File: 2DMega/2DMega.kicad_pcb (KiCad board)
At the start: 2 copper layers, 122.6 x 68.6 mm, 40 parts, among them J1 Conn_01x04_Male, J2 Conn_01x04_Female, J3 Conn_01x04_Male, J4 Conn_01x04_Female, P1 Power, P10 CONN_01X01, P11 CONN_01X01, P12 CONN_01X01, P13 CONN_01X01, P2 Analog, P3 Analog, P4 Digital, P5 PWM, P6 PWM, P7 Communication, P8 CONN_01X01, P9 CONN_01X01, U1 HDSP-A153

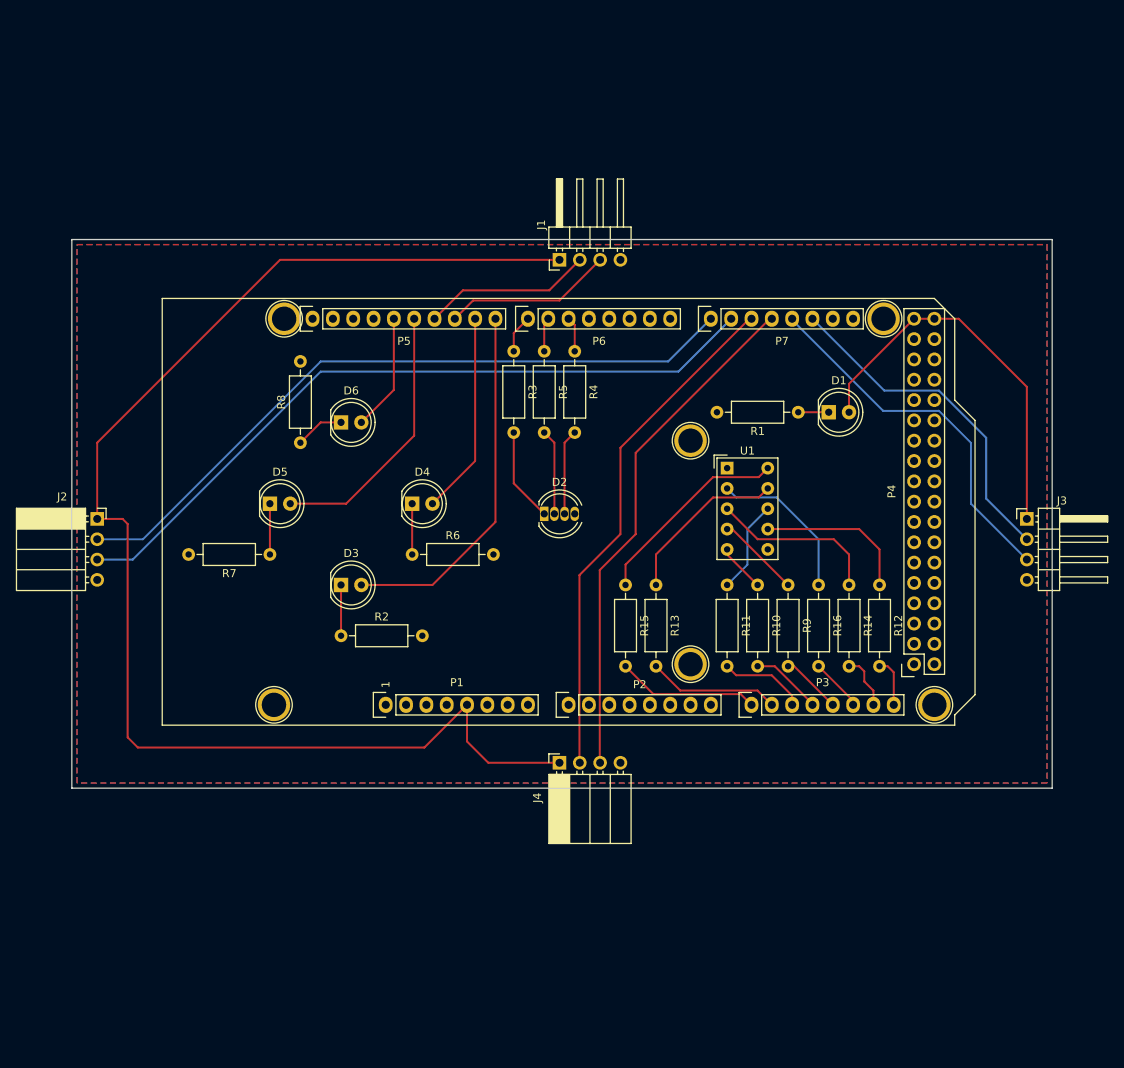
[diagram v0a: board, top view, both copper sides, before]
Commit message: Changed to square
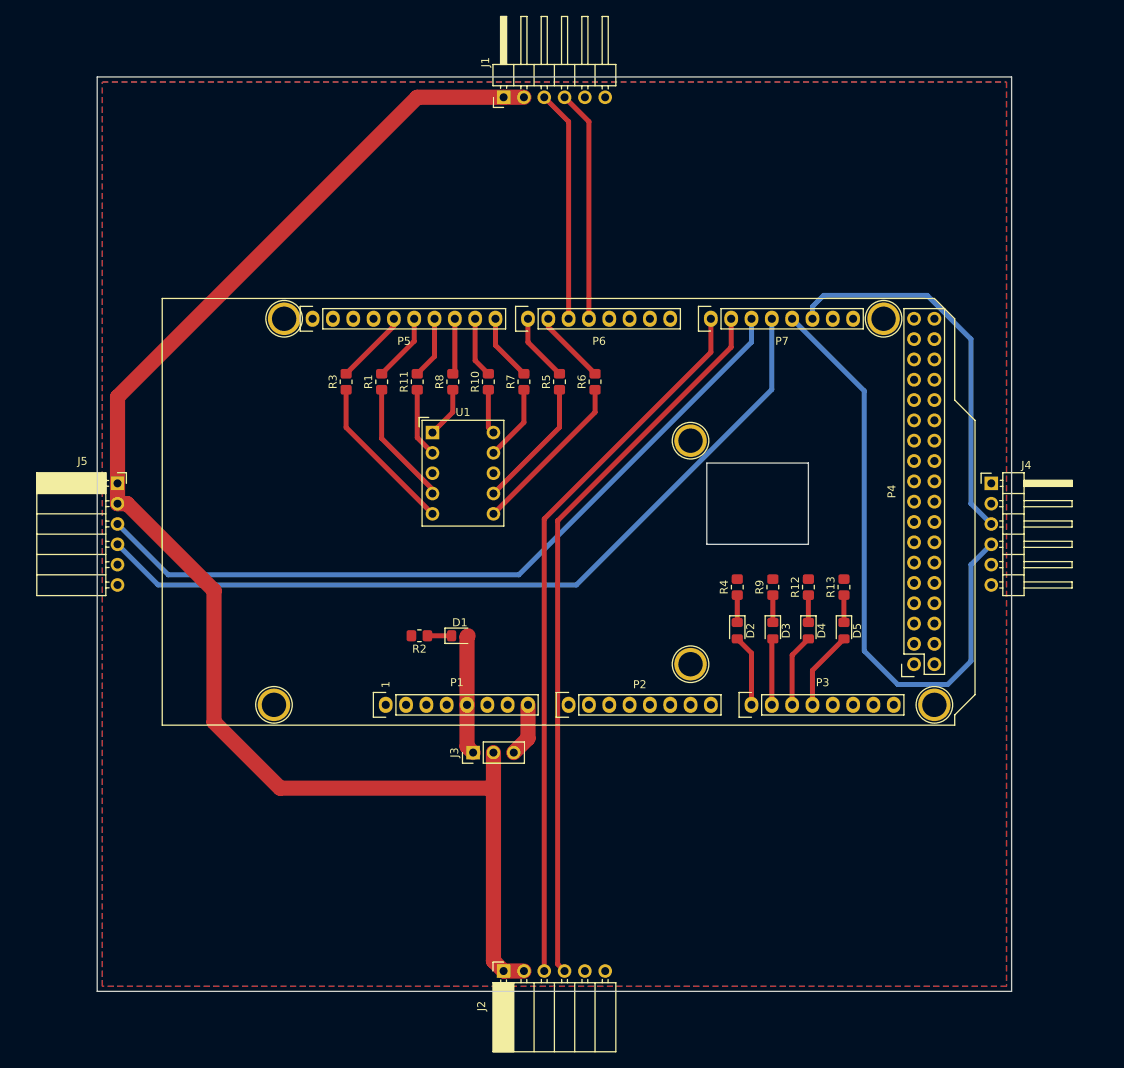
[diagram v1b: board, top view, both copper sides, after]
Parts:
- removed D6: LED, LED_THT:LED_D5.0mm
- removed R14, R15, R16: 330, Resistor_THT:R_Axial_DIN0207_L6.3mm_D2.5mm_P10.16mm_Horizontal
- added J5: Conn_01x06_Female, Connector_PinSocket_2.54mm:PinSocket_1x06_P2.54mm_Horizontal, F.Cu at (97.8, 91.4)
- D1, D3, D4, D5: footprint LED_THT:LED_D5.0mm -> LED_SMD:LED_0805_2012Metric_Pad1.15x1.40mm_HandSolder
- D2: value LED_RGBC -> LED; footprint LED_THT:LED_D5.0mm-4_RGB -> LED_SMD:LED_0805_2012Metric_Pad1.15x1.40mm_HandSolder
- J1: value Conn_01x04_Male -> Conn_01x06_Male; footprint Connector_PinHeader_2.54mm:PinHeader_1x04_P2.54mm_Horizontal -> Connector_PinHeader_2.54mm:PinHeader_1x06_P2.54mm_Horizontal
- J2: value Conn_01x04_Female -> Conn_01x06_Female; footprint Connector_PinSocket_2.54mm:PinSocket_1x04_P2.54mm_Horizontal -> Connector_PinSocket_2.54mm:PinSocket_1x06_P2.54mm_Horizontal
- J3: value Conn_01x04_Male -> Conn_01x03_Male; footprint Connector_PinHeader_2.54mm:PinHeader_1x04_P2.54mm_Horizontal -> Connector_PinHeader_2.54mm:PinHeader_1x03_P2.54mm_Vertical
- J4: value Conn_01x04_Female -> Conn_01x06_Male; footprint Connector_PinSocket_2.54mm:PinSocket_1x04_P2.54mm_Horizontal -> Connector_PinHeader_2.54mm:PinHeader_1x06_P2.54mm_Horizontal
- R1, R10, R11, R12, R13, R2, R3, R4, R5, R6, R7, R8, R9: value 330 -> 1k; footprint Resistor_THT:R_Axial_DIN0207_L6.3mm_D2.5mm_P10.16mm_Horizontal -> Resistor_SMD:R_0805_2012Metric_Pad1.20x1.40mm_HandSolder
- U1: value HDSP-A153 -> SC39-11YWA; footprint Display_7Segment:HDSP-A151 -> Display_7Segment:Sx39-1xxxxx
- moved J2 76.0 mm to (146.1, 152.4), turned to 90 degrees
- moved J3 75.1 mm to (142.2, 125.1), turned to 90 degrees
- moved D5 73.5 mm to (188.6, 109.9), turned to 270 degrees
- moved J4 64.3 mm to (207.0, 91.4), turned to 0 degrees
- moved D3 54.3 mm to (179.7, 109.9), turned to 270 degrees
- moved D1 53.9 mm to (140.6, 110.5)
- moved R1 52.2 mm to (130.8, 78.7), turned to 90 degrees
- moved D4 52.0 mm to (184.2, 109.9), turned to 270 degrees
- moved R11 46.3 mm to (135.3, 78.7), turned to 90 degrees
- moved R10 42.2 mm to (144.1, 78.7), turned to 90 degrees
- moved R7 38.4 mm to (148.6, 78.7), turned to 90 degrees
- moved U1 37.1 mm to (137.2, 85.1)
- moved R4 35.8 mm to (175.3, 104.4), turned to 90 degrees
- moved R6 31.4 mm to (157.5, 78.7), turned to 90 degrees
- moved D2 28.2 mm to (175.3, 109.9), turned to 270 degrees
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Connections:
- D2 pad 2: Net-(D2-Pad2) -> /A8
- D3 pad 2: /8(**) -> /A9
- D4 pad 2: /9(**) -> /A10
- D5 pad 2: /12(**) -> /A11
- J1 pad 1: +5V -> VCC
- J1 pad 2: /11(**) -> VCC
- J1 pad 3: /10(**) -> /5(**)
- J1 pad 4: GND -> /4(**)
- J2 pad 1: +5V -> VCC
- J2 pad 2: /14(Tx3) -> VCC
- J2 pad 3: /15(Rx3) -> /14(Tx3)
- J2 pad 4: GND -> /15(Rx3)
- J3 pad 2: /19(Rx1) -> VCC
- J3 pad 3: /18(Tx1) -> /Vin
- J4 pad 1: +5V -> VCC
- J4 pad 2: /16(Tx2) -> VCC
- J4 pad 3: /17(Rx2) -> /19(Rx1)
- J4 pad 4: GND -> /18(Tx1)
- R1 pad 1: Net-(D1-Pad1) -> Net-(R1-Pad1)
- R1 pad 2: GND -> /12(**)
- R10 pad 2: /A11 -> /9(**)
- R11 pad 2: /A10 -> /11(**)
- R12 pad 1: Net-(R12-Pad1) -> Net-(D4-Pad1)
- R12 pad 2: /A15 -> GND
- R13 pad 1: Net-(R13-Pad1) -> Net-(D5-Pad1)
- R13 pad 2: /A9 -> GND
- R2 pad 1: Net-(D3-Pad1) -> Net-(D1-Pad1)
- R3 pad 1: /7(**) -> Net-(R3-Pad1)
- R3 pad 2: Net-(D2-Pad1) -> /13(**)
- R4 pad 1: /5(**) -> Net-(D2-Pad1)
- R4 pad 2: Net-(D2-Pad3) -> GND
- R5 pad 1: /6(**) -> Net-(R5-Pad1)
- R5 pad 2: Net-(D2-Pad2) -> /7(**)
- R6 pad 1: Net-(D4-Pad1) -> Net-(R6-Pad1)
- R6 pad 2: GND -> /6(**)
- R7 pad 1: Net-(D5-Pad1) -> Net-(R7-Pad1)
- R7 pad 2: GND -> /8(**)
- R8 pad 1: Net-(D6-Pad1) -> Net-(R8-Pad1)
- R8 pad 2: GND -> /10(**)
- R9 pad 1: Net-(R9-Pad1) -> Net-(D3-Pad1)
- R9 pad 2: /A12 -> GND
- U1 pad 1: GND -> Net-(R8-Pad1)
- U1 pad 10: Net-(R15-Pad1) -> Net-(R10-Pad1)
- U1 pad 2: Net-(R16-Pad1) -> Net-(R11-Pad1)
- U1 pad 3: Net-(R14-Pad1) -> GND
- U1 pad 4: Net-(R9-Pad1) -> Net-(R1-Pad1)
- U1 pad 5: Net-(R10-Pad1) -> Net-(R3-Pad1)
- U1 pad 6: GND -> Net-(R6-Pad1)
- U1 pad 7: Net-(R12-Pad1) -> Net-(R5-Pad1)
- U1 pad 8: Net-(R11-Pad1) -> GND
- U1 pad 9: Net-(R13-Pad1) -> Net-(R7-Pad1)
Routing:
- net +5V: track 219.1 -> 15.0 mm
- net VCC: track 0.00 -> 181.4 mm
- net /17(Rx2): track 65.0 -> 103.2 mm
- net /8(**): track 45.4 -> 8.35 mm
- net /16(Tx2): track 64.9 -> 97.1 mm
- net /18(Tx1): track 46.3 -> 77.2 mm
- net /4(**): track 0.00 -> 28.9 mm
- net Net-(R15-Pad1): track 25.3 -> 0.00 mm
- net /12(**): track 34.3 -> 9.19 mm
- net /5(**): track 5.14 -> 29.7 mm
- net Net-(R14-Pad1): track 22.1 -> 0.00 mm
- net Net-(R13-Pad1): track 21.2 -> 0.00 mm
- net Net-(R6-Pad1): track 0.00 -> 20.8 mm
- net Net-(R3-Pad1): track 0.00 -> 20.0 mm
- net Net-(R16-Pad1): track 19.8 -> 0.00 mm
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- added copper zone on B.Cu, net VCC
- removed copper zone on B.Cu, net GND
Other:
- board size 122.6 x 68.6 mm -> 114.3 x 114.3 mm
- net class Default: trace_width 0.25 -> 0.625
- net class Power added: clearance 0.2, trace_width 1.9, via_dia 0.6, via_drill 0.4

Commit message: Added RGB_LED, reorganized pins
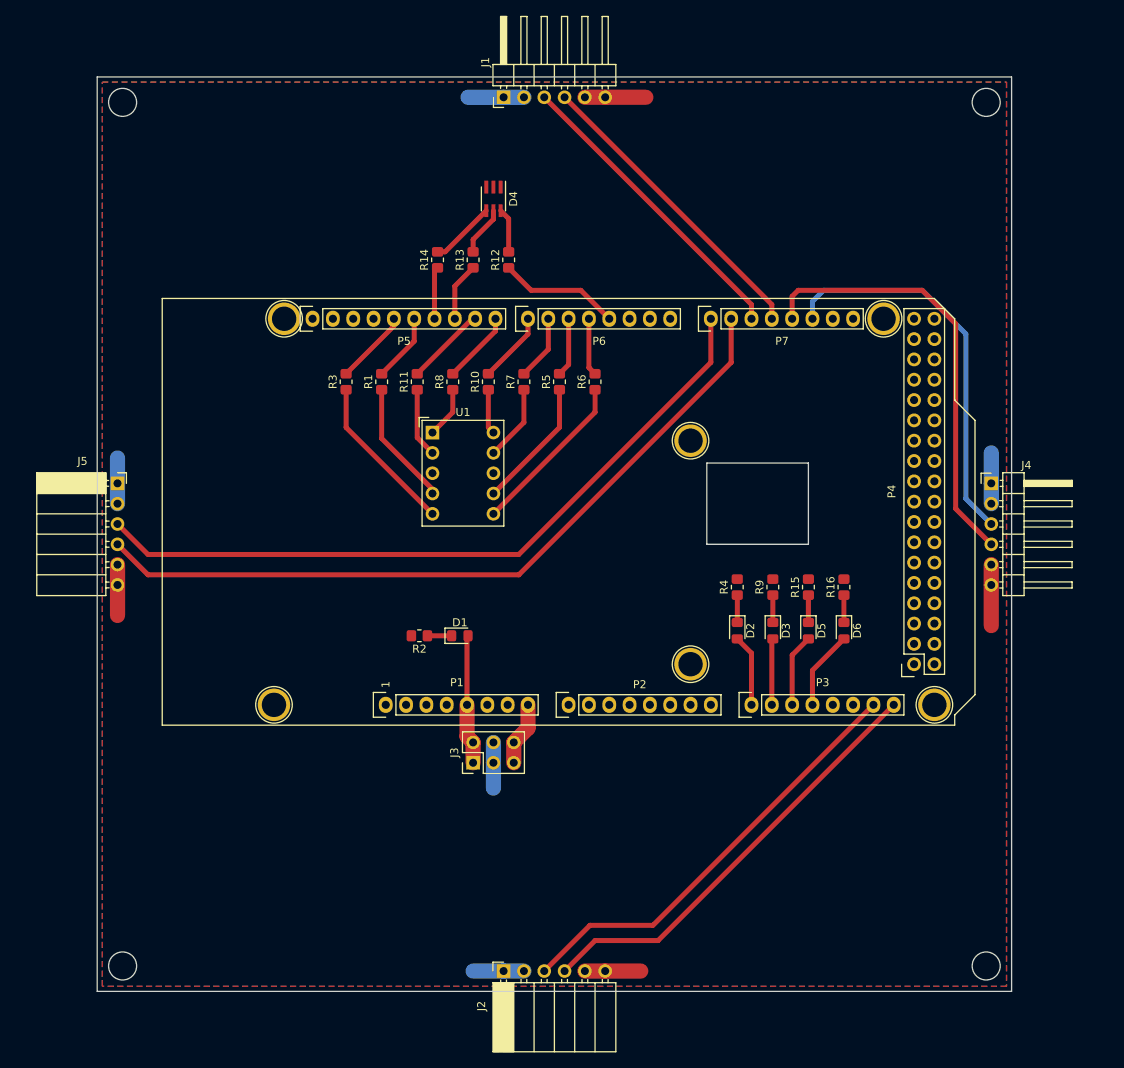
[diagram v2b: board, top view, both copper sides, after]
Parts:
- added D4: LED_RGB, LED_SMD:LED_Avago_PLCC6_3x2.8mm, F.Cu at (144.8, 55.9)
- added R12: 190, Resistor_SMD:R_0805_2012Metric_Pad1.20x1.40mm_HandSolder, F.Cu at (146.7, 63.5)
- added R13: 120, Resistor_SMD:R_0805_2012Metric_Pad1.20x1.40mm_HandSolder, F.Cu at (142.2, 63.5)
- added R14: 120, Resistor_SMD:R_0805_2012Metric_Pad1.20x1.40mm_HandSolder, F.Cu at (137.8, 63.5)
- J3: value Conn_01x03_Male -> Conn_02x03_Odd_Even; footprint Connector_PinHeader_2.54mm:PinHeader_1x03_P2.54mm_Vertical -> Connector_PinHeader_2.54mm:PinHeader_2x03_P2.54mm_Vertical
- R1, R10, R11, R3, R5, R6, R7, R8: value 1k -> 200
- moved J3 1.27 mm to (142.2, 126.4)
- renumbered D4 to D5, D5 to D6, R12 to R15, R13 to R16
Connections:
- J1 pad 3: /5(**) -> /16(Tx2)
- J1 pad 4: /4(**) -> /17(Rx2)
- J2 pad 3: /14(Tx3) -> /A14
- J2 pad 4: /15(Rx3) -> /A15
- J3 pad 2: VCC -> +5V
- J3 pad 3: /Vin -> VCC
- J5 pad 3: /16(Tx2) -> /14(Tx3)
- J5 pad 4: /17(Rx2) -> /15(Rx3)
- R10 pad 2: /9(**) -> /7(**)
- R11 pad 2: /11(**) -> /9(**)
- R5 pad 2: /7(**) -> /5(**)
- R6 pad 2: /6(**) -> /4(**)
- R7 pad 2: /8(**) -> /6(**)
- R8 pad 2: /10(**) -> /8(**)
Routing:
- net VCC: track 181.4 -> 31.1 mm
- net /17(Rx2): track 103.2 -> 38.8 mm
- net /16(Tx2): track 97.1 -> 38.7 mm
- net /A15: track 0.00 -> 54.9 mm
- net /A14: track 0.51 -> 55.4 mm
- net GND: track 0.00 -> 28.6 mm
- net /18(Tx1): track 77.2 -> 54.7 mm
- net /4(**): track 28.9 -> 7.19 mm
- net /5(**): track 29.7 -> 8.11 mm
- net /3(**): track 0.00 -> 15.2 mm
- net Net-(D4-Pad4): track 0.00 -> 8.22 mm
- net Net-(D4-Pad5): track 0.00 -> 6.20 mm
- net Net-(D4-Pad6): track 0.00 -> 5.56 mm
- net /15(Rx3): track 90.9 -> 94.7 mm
- net /9(**): track 7.56 -> 10.1 mm
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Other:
- outline, holes or cut-outs redrawn

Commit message: Added button and BOM
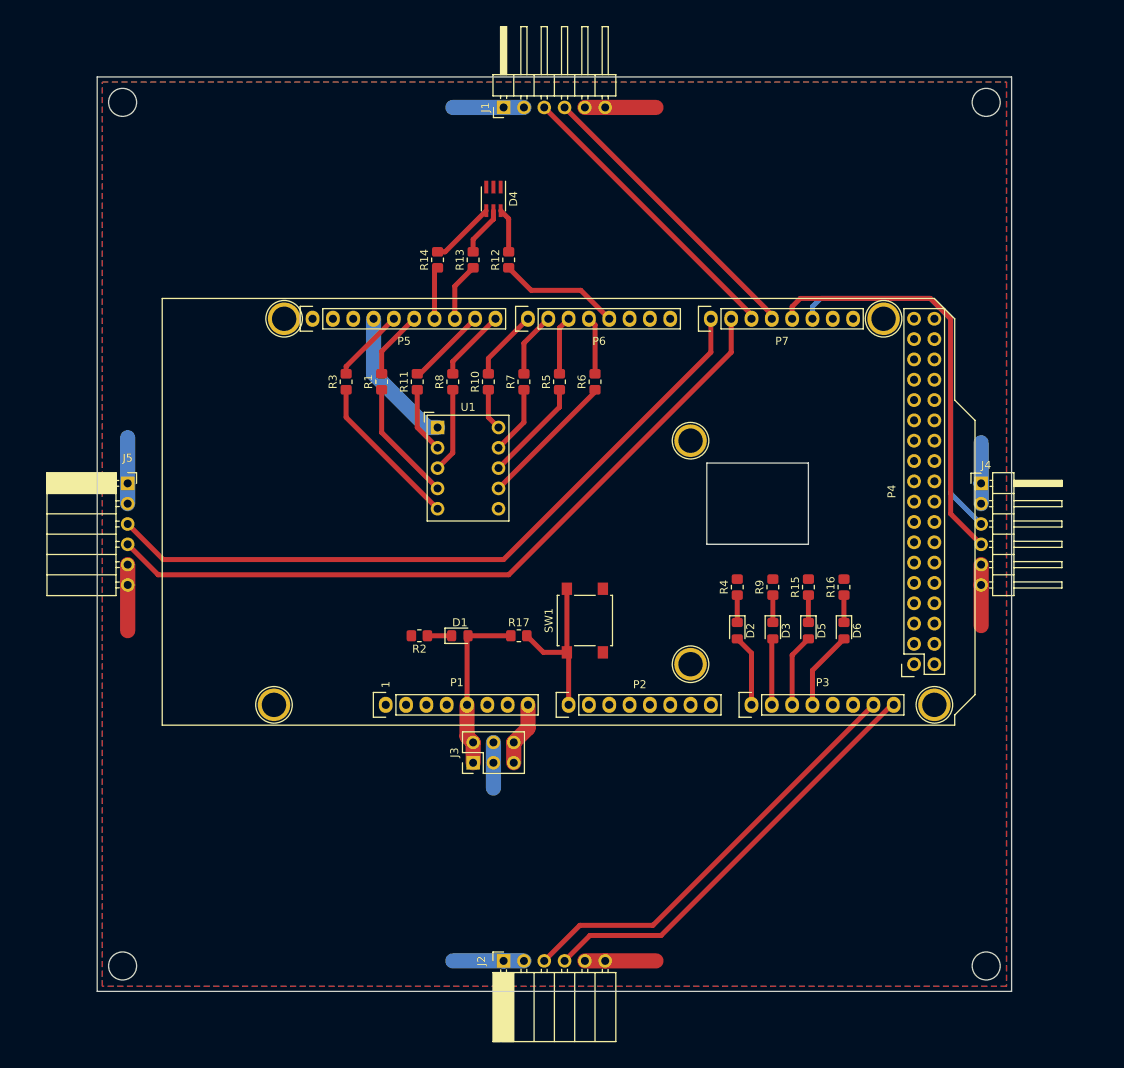
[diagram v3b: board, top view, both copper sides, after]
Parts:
- added R17: 10k, Resistor_SMD:R_0805_2012Metric_Pad1.20x1.40mm_HandSolder, F.Cu at (148.0, 110.5)
- added SW1: SW_SPST, Button_Switch_SMD:SW_SPST_B3S-1000, F.Cu at (156.2, 108.6)
- R12: value 190 -> 100
- R13: value 120 -> 100
- R14: value 120 -> 150
- R15, R16, R2, R4, R9: value 1k -> 150
- U1: value SC39-11YWA -> HDSP-A153
- moved J2 1.27 mm to (146.1, 151.1)
- moved J1 1.27 mm to (146.1, 44.5)
- moved J5 1.27 mm to (99.1, 91.4)
- moved J4 1.27 mm to (205.7, 91.4)
- moved U1 0.90 mm to (137.8, 84.5)
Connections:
- U1 pad 1: Net-(R8-Pad1) -> GND
- U1 pad 3: GND -> Net-(R8-Pad1)
- U1 pad 6: Net-(R6-Pad1) -> GND
- U1 pad 7: Net-(R5-Pad1) -> Net-(R6-Pad1)
- U1 pad 8: GND -> Net-(R5-Pad1)
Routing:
- net GND: track 28.6 -> 51.3 mm
- net /A0: track 0.00 -> 20.5 mm
- net VCC: track 31.1 -> 39.4 mm
- net +5V: track 16.2 -> 21.6 mm
- net Net-(R8-Pad1): track 6.40 -> 10.6 mm
- net Net-(R5-Pad1): track 16.4 -> 13.0 mm
- net Net-(R6-Pad1): track 20.8 -> 17.3 mm
- net /18(Tx1): track 54.7 -> 52.6 mm
- net /15(Rx3): track 94.7 -> 92.7 mm
- net /19(Rx1): track 49.2 -> 47.5 mm
- net /14(Tx3): track 91.5 -> 90.0 mm
- net /17(Rx2): track 38.8 -> 37.5 mm
- net /16(Tx2): track 38.7 -> 37.4 mm
- net Net-(R7-Pad1): track 9.47 -> 8.57 mm
- net /A15: track 54.9 -> 54.4 mm
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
